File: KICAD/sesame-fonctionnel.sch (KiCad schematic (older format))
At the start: 2 parts, among them J1 Screw_Terminal_01x04, J2 Screw_Terminal_01x04

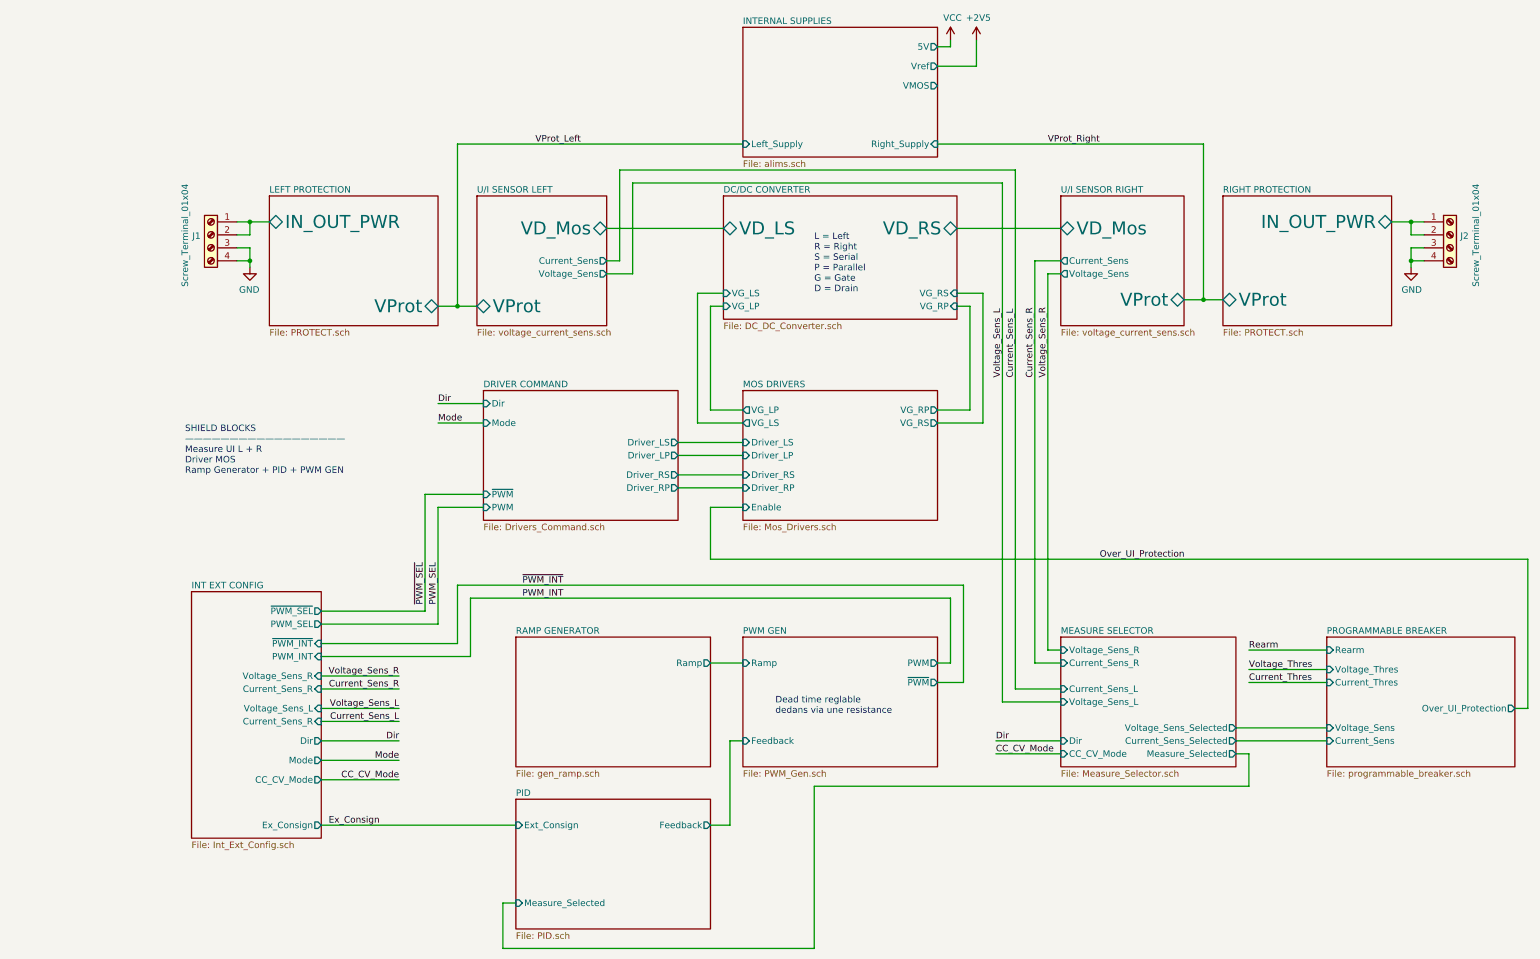
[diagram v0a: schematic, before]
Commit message: mod the main sheet + drawed the first full version of the u/i sensor
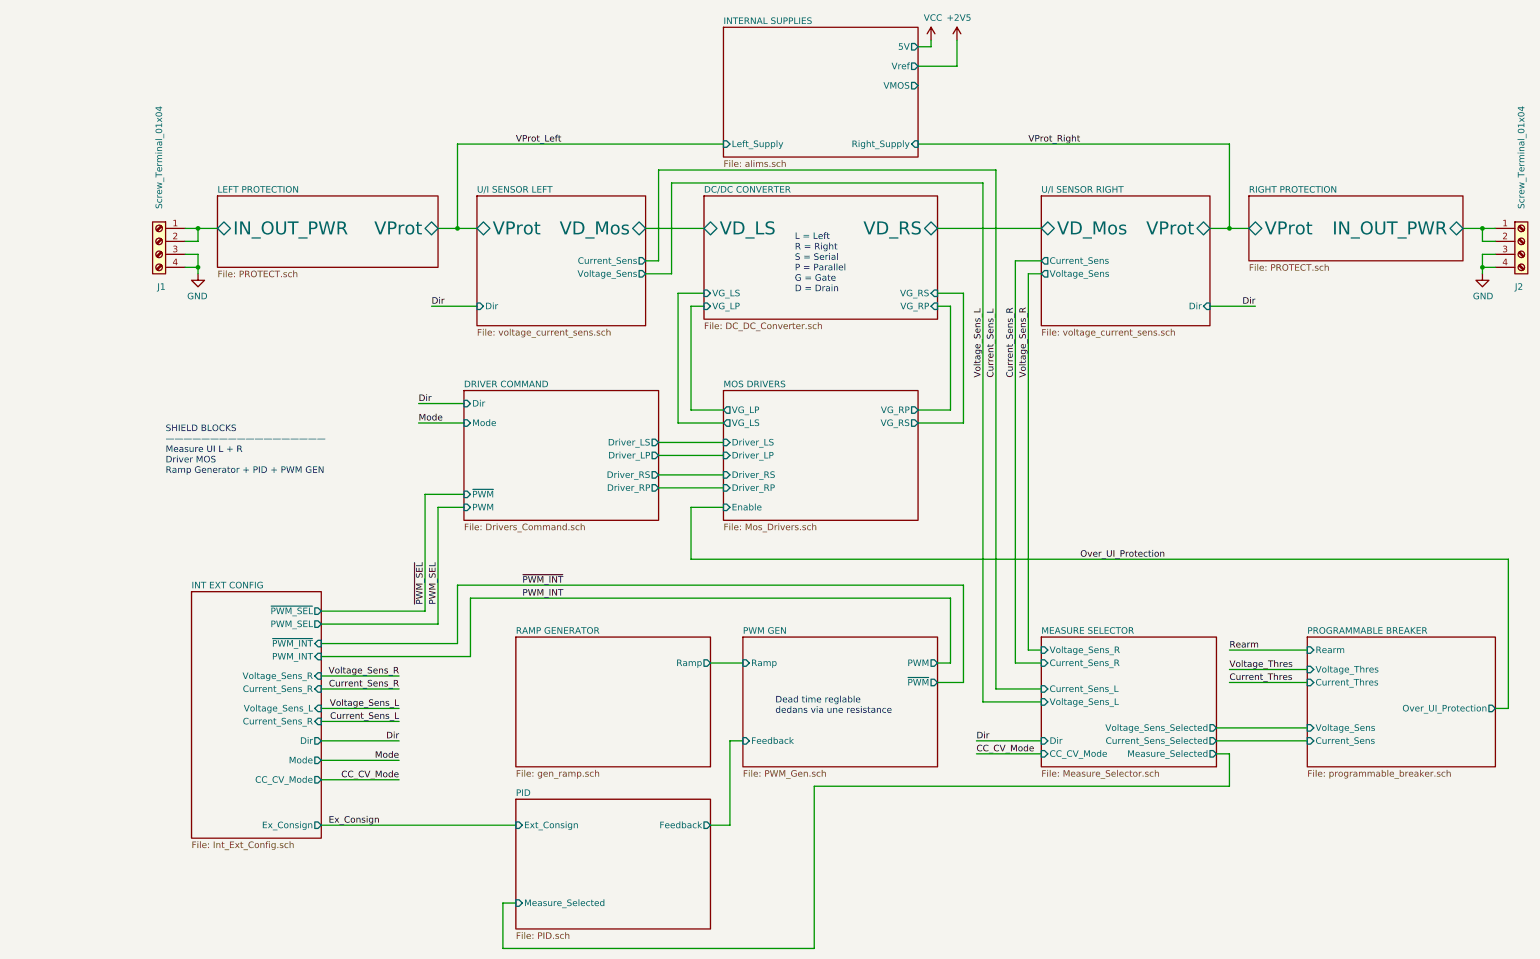
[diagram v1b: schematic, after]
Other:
- moved on the sheet: J1, J2

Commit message: minors edits + 7v rail
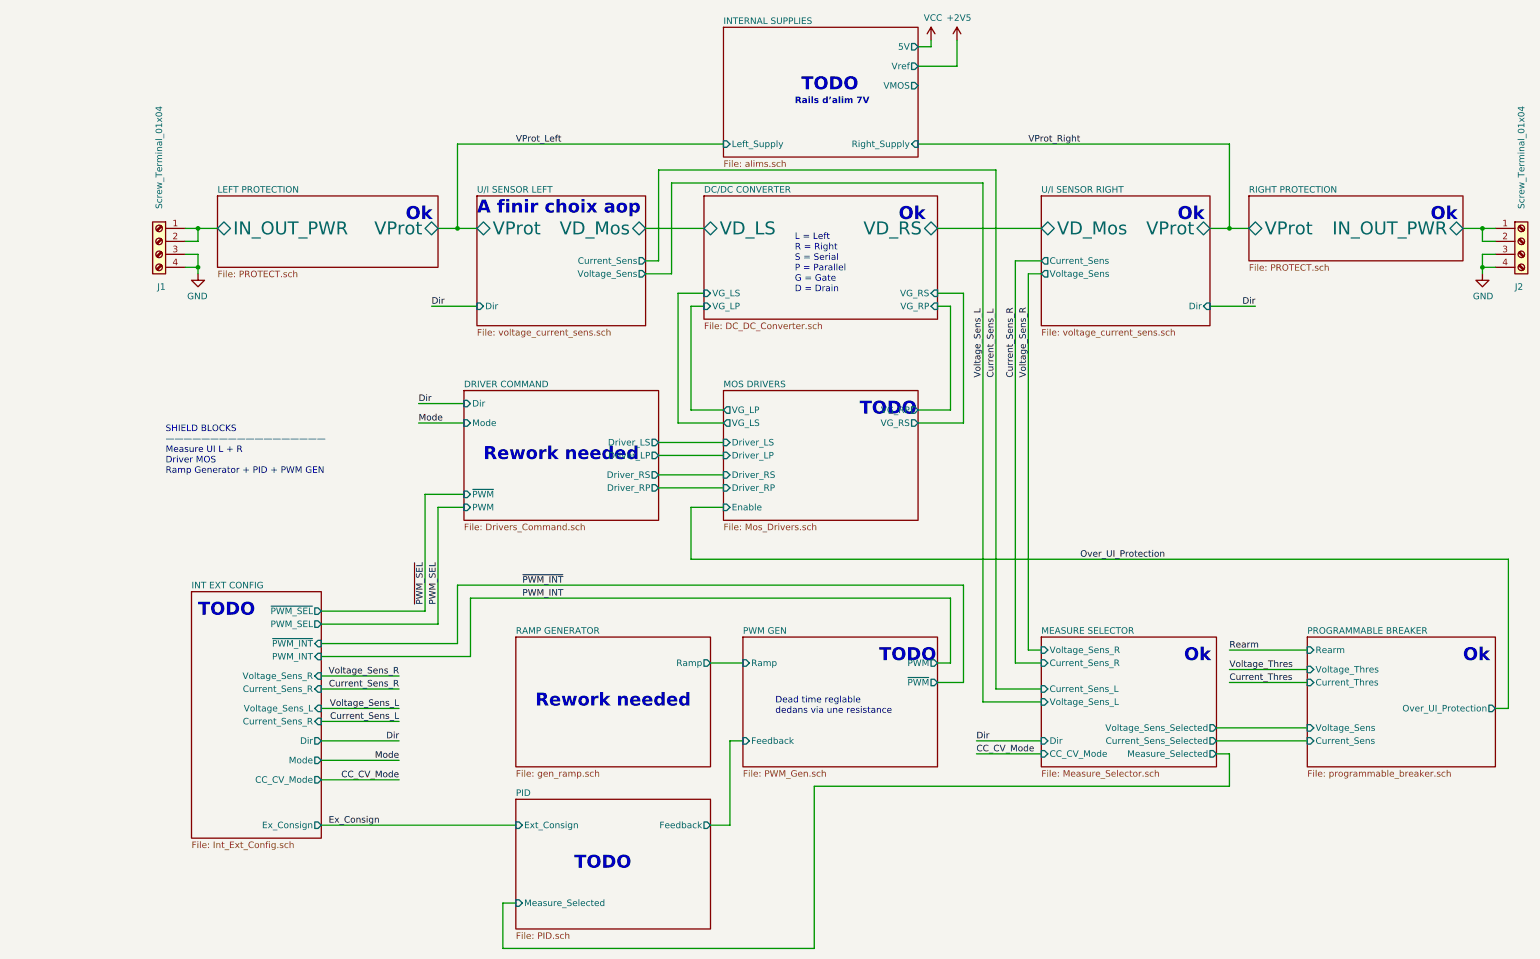
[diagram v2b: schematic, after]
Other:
- note added: "A finir choix aop"
- note added: "Ok"
- note added: "Rails d’alim 7V"
- note added: "Rework needed"
- note added: "TODO"
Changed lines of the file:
@@
 Wire Wire Line
 	9050 2800 8700 2800
+Text Notes 5550 1150 0    100  ~ 20
+TODO
+Text Notes 3100 4000 0    100  ~ 20
+Rework needed
+Text Notes 3500 5900 0    100  ~ 20
+Rework needed
+Text Notes 3800 7150 0    100  ~ 20
+TODO
+Text Notes 6150 5550 0    100  ~ 20
+TODO
+Text Notes 10650 5550 0    100  ~ 20
+Ok
+Text Notes 8500 5550 0    100  ~ 20
+Ok
+Text Notes 6300 2150 0    100  ~ 20
+Ok
+Text Notes 8450 2150 0    100  ~ 20
+Ok
+Text Notes 10400 2150 0    100  ~ 20
+Ok
+Text Notes 3050 2100 0    100  ~ 20
+A finir choix aop
+Text Notes 2500 2150 0    100  ~ 20
+Ok
+Text Notes 6000 3650 0    100  ~ 20
+TODO
+Text Notes 900  5200 0    100  ~ 20
+TODO
+Text Notes 5500 1250 0    50   ~ 10
+Rails d’alim 7V
 $EndSCHEMATC

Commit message: ebauche driver mos
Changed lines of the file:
@@
 F2 "VProt" B R 8700 2200 100
 F3 "VD_Mos" B L 7400 2200 100
-F4 "Current_Sens" O L 7400 2450 50
-F5 "Voltage_Sens" O L 7400 2550 50
+F4 "Current_Sens" O L 7400 2400 50
+F5 "Voltage_Sens" O L 7400 2500 50
 F6 "Dir" I R 8700 2800 50
 $EndSheet
@@
 F5 "Feedback" I L 5100 6150 50
 $EndSheet
-Wire Wire Line
-	7300 2550 7400 2550
-Wire Wire Line
-	7200 2450 7400 2450
 Wire Wire Line
 	6700 5050 6700 5550
@@
 	7400 5550 7200 5550
 Wire Wire Line
-	7400 5750 7050 5750
-$Comp
-L power:VCC #PWR0102
-U 1 1 61169F8F
-P 6550 750
-F 0 "#PWR0102" H 6550 600 50  0001 C CNN
-F 1 "VCC" H 6565 923 50  0000 C CNN
-F 2 "" H 6550 750 50  0001 C CNN
-F 3 "" H 6550 750 50  0001 C CNN
-	1    6550 750
-	1    0    0    -1
-$EndComp
-Wire Wire Line
-	6550 750  6550 800
-Wire Wire Line
-	6550 800  6450 800
-$Comp
-L power:+2V5 #PWR0103
-U 1 1 6117E6E2
-P 6750 750
-F 0 "#PWR0103" H 6750 600 50  0001 C CNN
-F 1 "+2V5" H 6765 923 50  0000 C CNN
-F 2 "" H 6750 750 50  0001 C CNN
-F 3 "" H 6750 750 50  0001 C CNN
-	1    6750 750
-	1    0    0    -1
-$EndComp
-Wire Wire Line
-	6750 750  6750 950
-Wire Wire Line
-	6750 950  6450 950
-Wire Wire Line
-	6950 5850 7400 5850
+	7400 5750 7100 5750
+Wire Wire Line
+	7000 5850 7400 5850
 Wire Wire Line
 	5650 6500 5650 7750
@@
 Dead time reglable\ndedans via une resistance
 Wire Wire Line
-	4450 1750 4450 2450
+	4450 1750 4450 2400
 $Sheet
 S 1050 1950 1700 550
@@
 $EndSheet
 Wire Wire Line
-	4550 1850 4550 2550
+	4550 1850 4550 2500
 Connection ~ 900  2500
 Wire Wire Line
@@
 	2900 4950 6800 4950
 Wire Wire Line
-	4450 3950 4950 3950
+	4450 4000 4950 4000
 Wire Wire Line
 	4950 4100 4450 4100
 Wire Wire Line
 	4450 4200 4950 4200
-Wire Wire Line
-	4450 2450 4350 2450
-Wire Wire Line
-	4550 2550 4350 2550
 Wire Wire Line
 	10650 2200 10800 2200
@@
 F2 "VD_LS" B L 4800 2200 100
 F3 "VD_RS" B R 6600 2200 100
-F4 "VG_LS" I L 4800 2700 50
+F4 "VG_LS" I L 4800 2600 50
 F5 "VG_LP" I L 4800 2800 50
-F6 "VG_RS" I R 6600 2700 50
+F6 "VG_RS" I R 6600 2600 50
 F7 "VG_RP" I R 6600 2800 50
+F8 "VS_L" U L 4800 2700 50
+F9 "VS_R" U R 6600 2700 50
 $EndSheet
 Text Notes 5500 2700 0    50   ~ 0
 L = Left\nR = Right\nS = Serial\nP = Parallel \nG = Gate\nD = Drain
 Wire Wire Line
-	6800 2700 6800 3700
-Wire Wire Line
-	6450 3700 6800 3700
-Wire Wire Line
-	6600 2800 6700 2800
-Wire Wire Line
-	6700 2800 6700 3600
-Wire Wire Line
-	6450 3600 6700 3600
-Wire Wire Line
-	4600 3700 4600 2700
-Wire Wire Line
-	4600 3700 4950 3700
-Wire Wire Line
-	4800 2800 4700 2800
-Wire Wire Line
-	4700 2800 4700 3600
-Wire Wire Line
-	4700 3600 4950 3600
-Wire Wire Line
-	4800 2700 4600 2700
-Wire Wire Line
-	6800 2700 6600 2700
+	6600 2800 6650 2800
+Wire Wire Line
+	4650 3750 4950 3750
+Wire Wire Line
+	4800 2800 4750 2800
+Wire Wire Line
+	4750 2800 4750 3550
+Wire Wire Line
+	6700 2700 6600 2700
 $Sheet
 S 850  5000 1000 1900
@@
 Text Label 7200 3350 1    50   ~ 0
 Current_Sens_R
-Text Label 7050 3350 1    50   ~ 0
+Text Label 7100 3350 1    50   ~ 0
 Current_Sens_L
-Text Label 6950 3350 1    50   ~ 0
+Text Label 7000 3350 1    50   ~ 0
 Voltage_Sens_L
 Text Label 7700 4750 0    50   ~ 0
@@
 $EndSheet
 Wire Wire Line
-	7200 2450 7200 5550
-Wire Wire Line
-	7300 2550 7300 5450
-Wire Wire Line
-	6950 1850 6950 5850
+	7200 2400 7200 5550
+Wire Wire Line
+	7300 2500 7300 5450
+Wire Wire Line
+	7000 1850 7000 5850
 Wire Wire Line
 	8750 6250 8850 6250
@@
 Current_Sens_L
 Wire Wire Line
-	4450 1750 7050 1750
-Wire Wire Line
-	4550 1850 6950 1850
+	4450 1750 7100 1750
+Wire Wire Line
+	4550 1850 7000 1850
 Wire Wire Line
 	5650 6500 8850 6500
@@
 F2 "VProt" B L 3050 2200 100
 F3 "VD_Mos" B R 4350 2200 100
-F4 "Current_Sens" O R 4350 2450 50
-F5 "Voltage_Sens" O R 4350 2550 50
+F4 "Current_Sens" O R 4350 2400 50
+F5 "Voltage_Sens" O R 4350 2500 50
 F6 "Dir" I L 3050 2800 50
 $EndSheet
 Wire Wire Line
-	7050 1750 7050 5750
+	7100 1750 7100 5750
 Text Label 6900 6150 0    50   ~ 0
 Dir
@@
 	4700 4350 4700 4750
 Wire Wire Line
-	4450 3850 4950 3850
+	4450 3900 4950 3900
 $Sheet
 S 2950 3450 1500 1000
@@
 F0 "DRIVER COMMAND" 50
 F1 "Drivers_Command.sch" 50
-F2 "Driver_LS" O R 4450 3850 50
-F3 "Driver_LP" O R 4450 3950 50
+F2 "Driver_LS" O R 4450 3900 50
+F3 "Driver_LP" O R 4450 4000 50
 F4 "Driver_RS" O R 4450 4100 50
 F5 "Driver_RP" O R 4450 4200 50
@@
 F0 "INTERNAL SUPPLIES" 50
 F1 "alims.sch" 50
-F2 "5V" O R 6450 800 50
-F3 "Vref" O R 6450 950 50
-F4 "VMOS" O R 6450 1100 50
-F5 "Left_Supply" I L 4950 1550 50
-F6 "Right_Supply" I R 6450 1550 50
+F2 "Left_Supply" I L 4950 1550 50
+F3 "Right_Supply" I R 6450 1550 50
 $EndSheet
 $Sheet
@@
 F0 "MOS DRIVERS" 50
 F1 "Mos_Drivers.sch" 50
-F2 "Driver_LS" I L 4950 3850 50
-F3 "VG_LP" O L 4950 3600 50
-F4 "Driver_LP" I L 4950 3950 50
-F5 "VG_LS" O L 4950 3700 50
-F6 "VG_RS" O R 6450 3700 50
-F7 "VG_RP" O R 6450 3600 50
+F2 "Driver_LS" I L 4950 3900 50
+F3 "VG_LP" O L 4950 3550 50
+F4 "Driver_LP" I L 4950 4000 50
+F5 "VG_LS" O L 4950 3750 50
+F6 "VG_RS" O R 6450 3750 50
+F7 "VG_RP" O R 6450 3550 50
 F8 "Driver_RP" I L 4950 4200 50
 F9 "Driver_RS" I L 4950 4100 50
 F10 "Enable" I L 4950 4350 50
+F12 "VS_L" U L 4950 3650 50
+F13 "VS_R" U R 6450 3650 50
 $EndSheet
 Wire Wire Line
@@
 Text Notes 2500 2150 0    100  ~ 20
 Ok
-Text Notes 6000 3650 0    100  ~ 20
+Text Notes 6000 4400 0    100  ~ 20
 TODO
 Text Notes 900  5200 0    100  ~ 20
@@
 Text Notes 5500 1250 0    50   ~ 10
 Rails d’alim 7V
+Wire Wire Line
+	4950 3550 4750 3550
+Wire Wire Line
+	4800 2600 4650 2600
+Wire Wire Line
+	4650 2600 4650 3750
+Wire Wire Line
+	4700 2700 4800 2700
+Wire Wire Line
+	4700 2700 4700 3650
+Wire Wire Line
+	4950 3650 4700 3650
+Wire Wire Line
+	6650 2800 6650 3550
+Wire Wire Line
+	6450 3550 6650 3550
+Wire Wire Line
+	4350 2400 4450 2400
+Wire Wire Line
+	4350 2500 4550 2500
+Wire Wire Line
+	7200 2400 7400 2400
+Wire Wire Line
+	7300 2500 7400 2500
+Wire Wire Line
+	6600 2600 6750 2600
+Wire Wire Line
+	6750 2600 6750 3750
+Wire Wire Line
+	6450 3750 6750 3750
+Wire Wire Line
+	6450 3650 6700 3650
+Wire Wire Line
+	6700 3650 6700 2700
 $EndSCHEMATC

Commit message: added draft pwm gen & pid
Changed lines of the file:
@@
 Wire Wire Line
 	9050 2800 8700 2800
-Text Notes 5550 1150 0    100  ~ 20
+Text Notes 5450 900  0    100  ~ 20
 TODO
-Text Notes 3100 4000 0    100  ~ 20
+Text Notes 3250 3650 0    100  ~ 20
 Rework needed
 Text Notes 3500 5900 0    100  ~ 20
 Rework needed
-Text Notes 3800 7150 0    100  ~ 20
-TODO
-Text Notes 6150 5550 0    100  ~ 20
-TODO
 Text Notes 10650 5550 0    100  ~ 20
 Ok
 Text Notes 8500 5550 0    100  ~ 20
 Ok
-Text Notes 6300 2150 0    100  ~ 20
+Text Notes 5550 2150 0    100  ~ 20
 Ok
 Text Notes 8450 2150 0    100  ~ 20
@@
 Text Notes 2500 2150 0    100  ~ 20
 Ok
-Text Notes 6000 4400 0    100  ~ 20
-TODO
 Text Notes 900  5200 0    100  ~ 20
 TODO
-Text Notes 5500 1250 0    50   ~ 10
+Text Notes 5400 1000 0    50   ~ 10
 Rails d’alim 7V
 Wire Wire Line
@@
 Wire Wire Line
 	6700 3650 6700 2700
+Text Notes 5300 5750 0    100  ~ 20
+Rework needed
+Text Notes 3500 7200 0    100  ~ 20
+Rework needed
+Text Notes 5150 4250 0    100  ~ 20
+Rework needed
 $EndSCHEMATC

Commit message: a ton of new stuff. V0.8
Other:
- note added: "Presque ok"
- note added: "Trouver Driver"
- note removed: "SHIELD BLOCKS\n——————————————————\nMeasure UI L + R\nDriver MOS\nRamp Generator + PID + PWM GEN\n"
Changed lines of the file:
@@
 $Descr A4 11693 8268
 encoding utf-8
-Sheet 1 15
+Sheet 1 16
 Title "SESAME"
-Date "2021-07-26"
-Rev "0.7"
+Date "2021-08-17"
+Rev "0.8"
 Comp "ALEEA"
 Comment1 "Dessin : Guillaume Arthaud"
@@
 	7000 5850 7400 5850
 Wire Wire Line
-	5650 6500 5650 7750
-Wire Wire Line
-	3250 7750 5650 7750
+	5950 6500 5950 7750
+Wire Wire Line
+	3250 7750 5950 7750
 $Sheet
 S 9000 1950 1650 500
@@
 F4 "Ext_Consign" I L 3350 6800 50
 $EndSheet
-Text Notes 650  4100 0    50   ~ 0
-SHIELD BLOCKS\n——————————————————\nMeasure UI L + R\nDriver MOS\nRamp Generator + PID + PWM GEN\n
 $Sheet
 S 9450 5350 1450 1000
@@
 	4550 1850 7000 1850
 Wire Wire Line
-	5650 6500 8850 6500
+	5950 6500 8850 6500
 Wire Wire Line
 	11000 4750 11000 5900
@@
 F9 "Driver_RS" I L 4950 4100 50
 F10 "Enable" I L 4950 4350 50
-F12 "VS_L" U L 4950 3650 50
-F13 "VS_R" U R 6450 3650 50
+F11 "VS_L" U L 4950 3650 50
+F12 "VS_R" U R 6450 3650 50
 $EndSheet
 Wire Wire Line
@@
 Text Notes 3250 3650 0    100  ~ 20
 Rework needed
-Text Notes 3500 5900 0    100  ~ 20
-Rework needed
-Text Notes 10650 5550 0    100  ~ 20
-Ok
+Text Notes 3600 5900 0    100  ~ 20
+Presque ok
+Text Notes 9950 5550 0    100  ~ 20
+Presque ok
 Text Notes 8500 5550 0    100  ~ 20
 Ok
 Text Notes 5550 2150 0    100  ~ 20
 Ok
-Text Notes 8450 2150 0    100  ~ 20
-Ok
-Text Notes 10400 2150 0    100  ~ 20
-Ok
 Text Notes 3050 2100 0    100  ~ 20
 A finir choix aop
-Text Notes 2500 2150 0    100  ~ 20
-Ok
 Text Notes 900  5200 0    100  ~ 20
 TODO
@@
 Text Notes 3500 7200 0    100  ~ 20
 Rework needed
-Text Notes 5150 4250 0    100  ~ 20
-Rework needed
+Text Notes 5250 4400 0    100  ~ 20
+Trouver Driver
+Text Notes 7400 2100 0    100  ~ 20
+A finir choix aop
+$Sheet
+S 650  700  500  150
+U 6142ECA0
+F0 "INFOS" 100
+F1 "infos.sch" 100
+$EndSheet
 $EndSCHEMATC
